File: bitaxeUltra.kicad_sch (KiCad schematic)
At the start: 17 parts, among them J1 PJ-037AH, J6 PJ-037AH

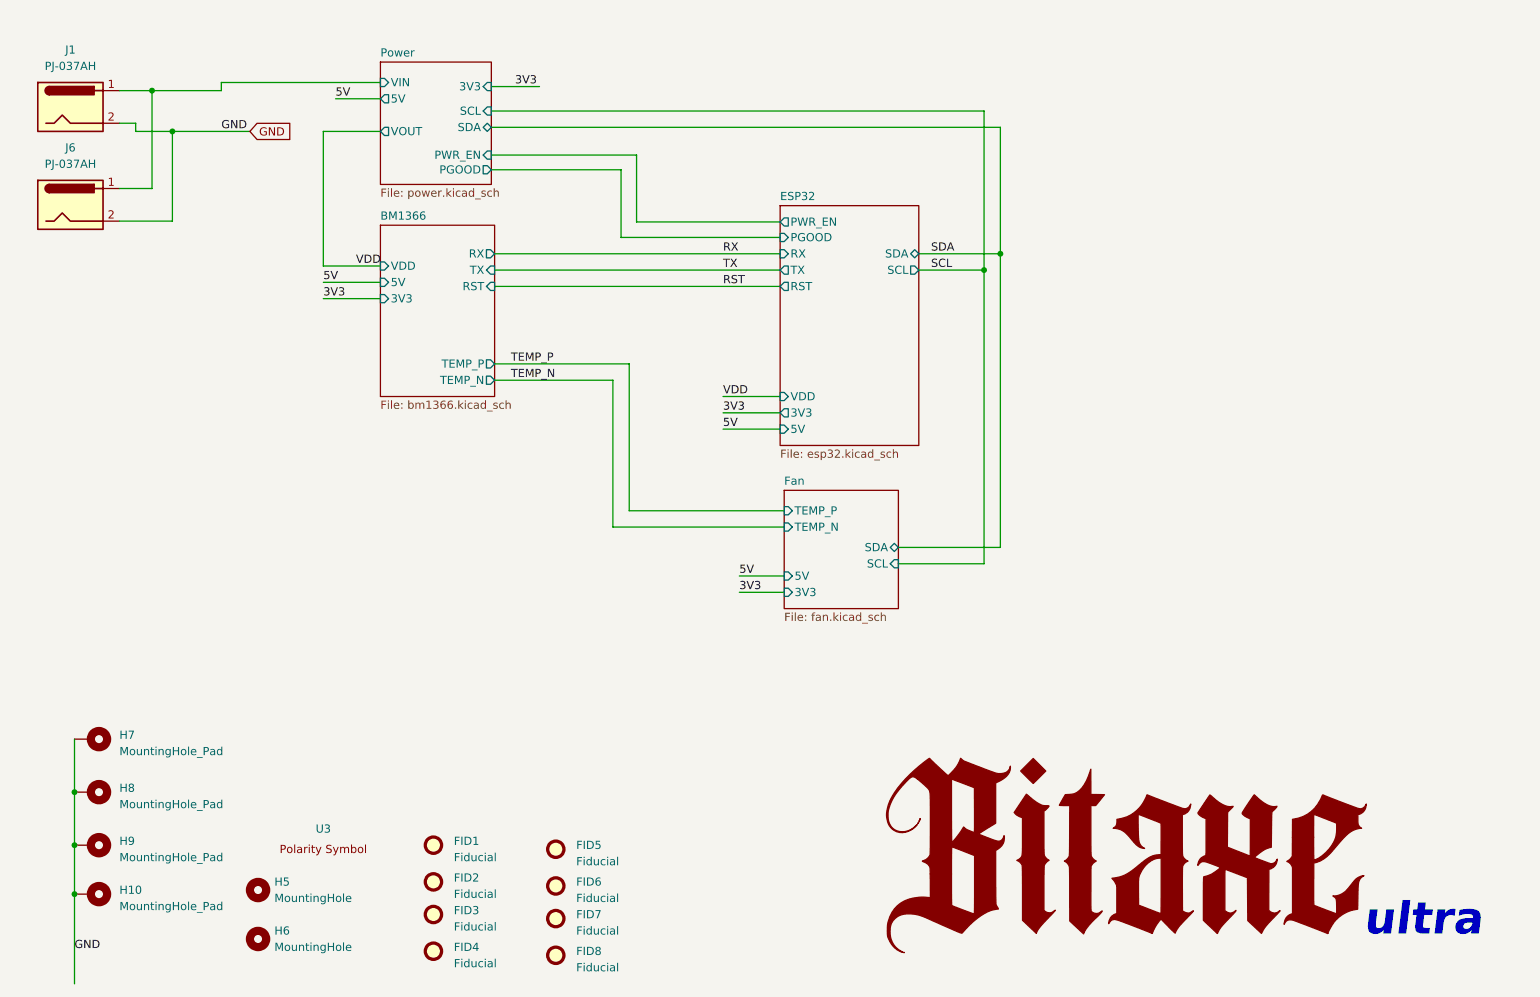
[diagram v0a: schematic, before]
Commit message: added bitaxe variant for rasperry pi
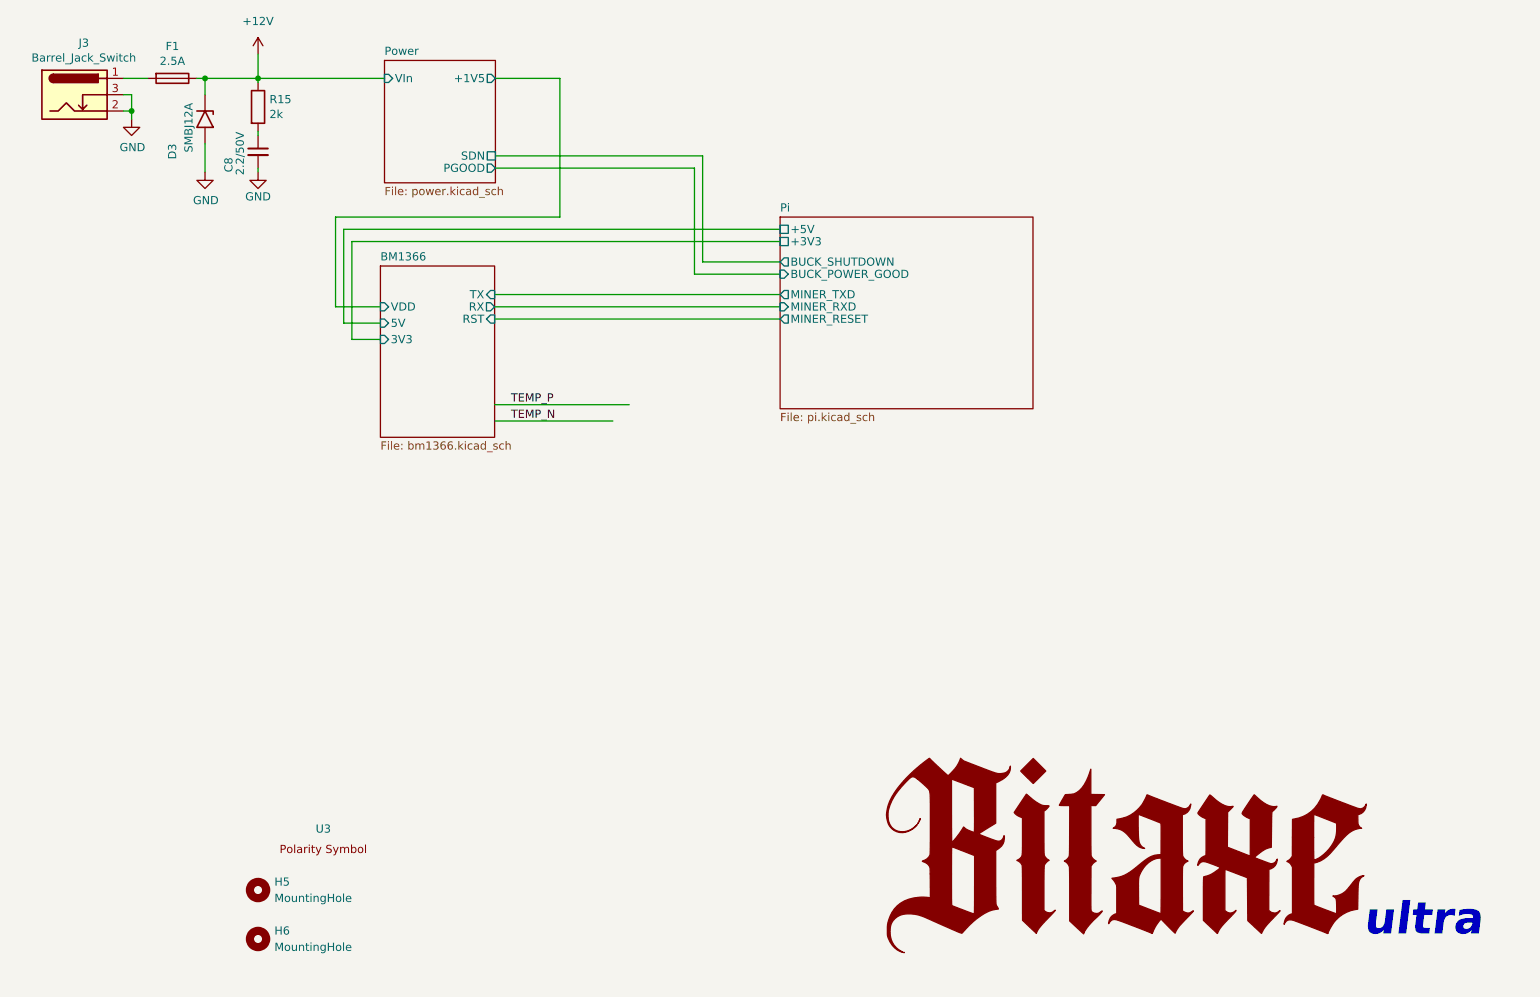
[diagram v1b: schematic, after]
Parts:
- removed FID1, FID2, FID3, FID4, FID5, FID6, FID7, FID8: Fiducial, Fiducial:Fiducial_1mm_Mask2mm, symbol Mechanical:Fiducial
- removed H10, H7, H8, H9: MountingHole_Pad, MountingHole:MountingHole_3mm_Pad_Via, symbol Mechanical:MountingHole_Pad
- removed J1, J6: PJ-037AH, bitaxe:CUI_PJ-037AH, symbol Connector:Barrel_Jack
- added C8: 2.2/50V, Capacitor_SMD:C_1206_3216Metric, symbol Device:C_Small
- added D3: SMBJ12A, Diode_SMD:D_SMB, symbol Diode:5KPxxA
- added F1: 2.5A, myfootprints:fuseholder_littlefuse_blok, symbol Device:Fuse
- added J3: Barrel_Jack_Switch, Connector_BarrelJack:BarrelJack_CUI_PJ-102AH_Horizontal, symbol Connector:Barrel_Jack_Switch
- added R15: 2k, Resistor_SMD:R_0805_2012Metric, symbol Device:R
- H5, H6, U3: Distributor (none) -> -
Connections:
- net GND: now also C8.2, D3.2 (A2), J3.2, J3.3
- new net: F1.2, J3.1
- new net: C8.1, R15.2
- new net +12V: D3.1 (A1), F1.1, R15.1
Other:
- removed sheet ESP32
- removed sheet Fan
- added sheet Pi (pi.kicad_sch)
- sheet BM1366 ports: added none; removed TEMP_N, TEMP_P
- sheet Power ports: added +1V5, SDN, VIn; removed 3V3, 5V, PWR_EN, SCL, SDA, VIN, VOUT
